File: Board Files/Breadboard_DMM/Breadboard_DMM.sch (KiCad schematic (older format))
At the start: 8 parts

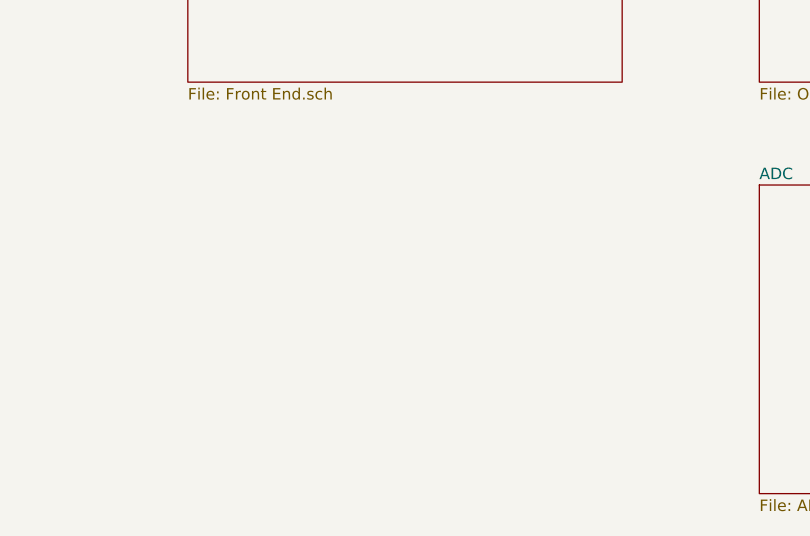
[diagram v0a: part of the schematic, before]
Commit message: Started cleaning up front end page
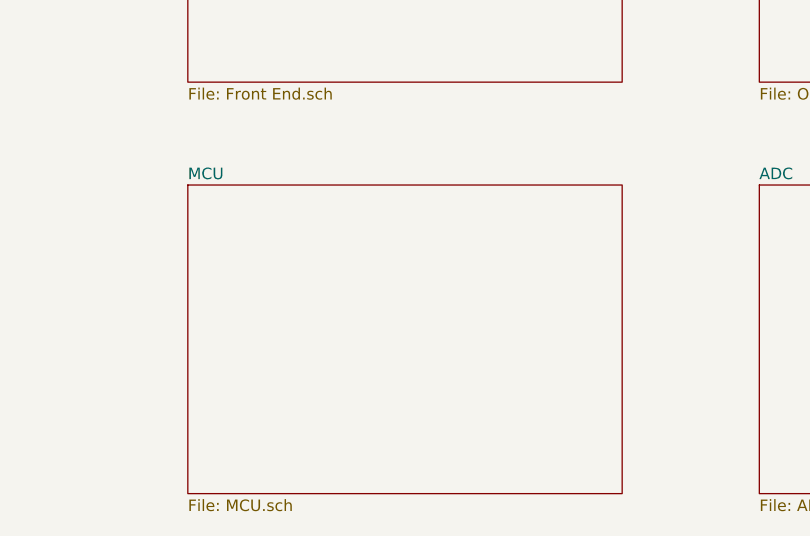
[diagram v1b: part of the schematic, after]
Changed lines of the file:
@@
 $Descr USLetter 11000 8500
 encoding utf-8
-Sheet 1 4
+Sheet 1 6
 Title "Toast-O-Meter"
 Date "2020-08-14"
@@
 F1 "ADC.sch" 50
 $EndSheet
+$Sheet
+S 1850 4700 1900 1350
+U 5F3FD151
+F0 "MCU" 50
+F1 "MCU.sch" 50
+$EndSheet
 $EndSCHEMATC

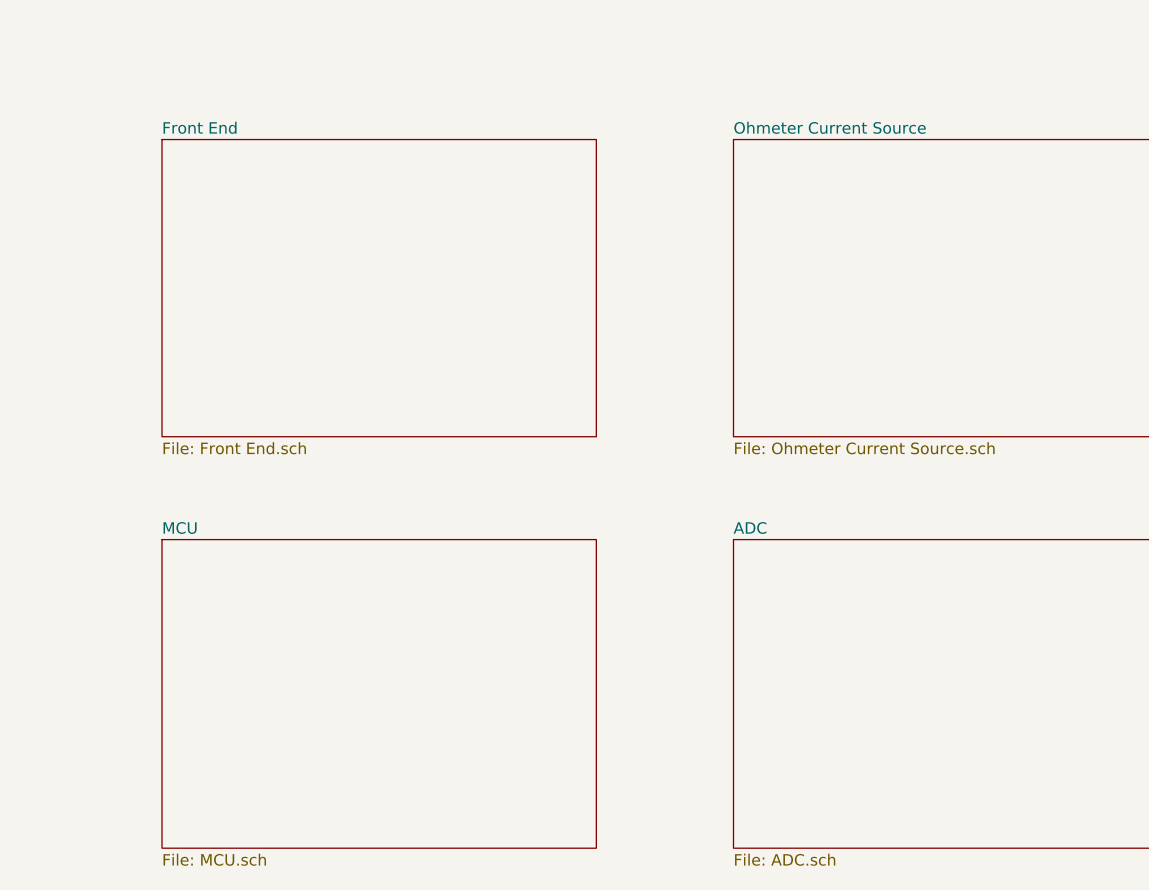
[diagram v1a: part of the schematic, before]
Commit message: Starting converting to hierachichal design
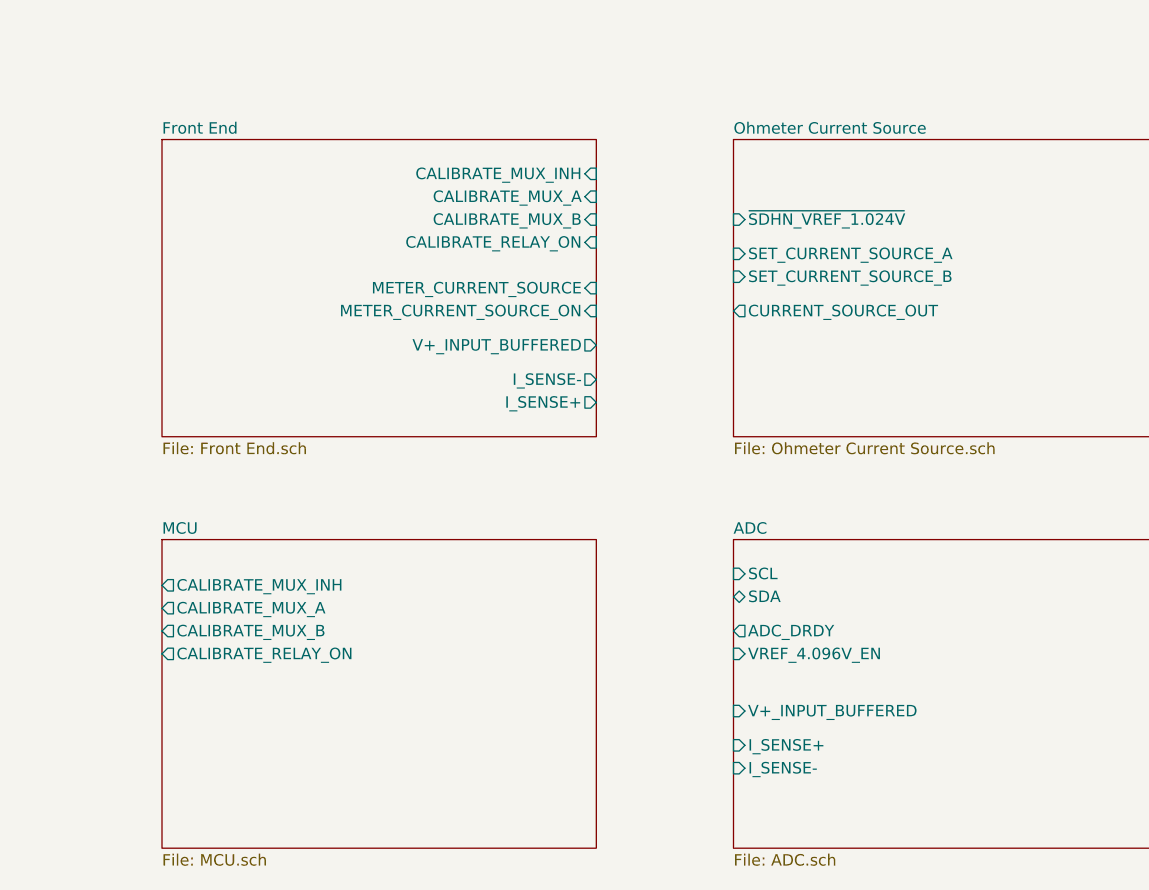
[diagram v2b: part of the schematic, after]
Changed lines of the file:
@@
 $EndComp
+$Sheet
+S 1850 4700 1900 1350
+U 5F3FD151
+F0 "MCU" 50
+F1 "MCU.sch" 50
+F2 "CALIBRATE_MUX_INH" O L 1850 4900 50
+F3 "CALIBRATE_MUX_A" O L 1850 5000 50
+F4 "CALIBRATE_MUX_B" O L 1850 5100 50
+F5 "CALIBRATE_RELAY_ON" O L 1850 5200 50
+$EndSheet
+$Sheet
+S 4350 4700 1900 1350
+U 5FDFAE85
+F0 "ADC" 50
+F1 "ADC.sch" 50
+F2 "V+_INPUT_BUFFERED" I L 4350 5450 50
+F3 "I_SENSE+" I L 4350 5600 50
+F4 "I_SENSE-" I L 4350 5700 50
+F5 "VREF_4.096V_EN" I L 4350 5200 50
+F6 "SCL" I L 4350 4850 50
+F7 "SDA" B L 4350 4950 50
+F8 "ADC_DRDY" O L 4350 5100 50
+$EndSheet
 $Sheet
 S 1850 2950 1900 1300
@@
 F0 "Front End" 50
 F1 "Front End.sch" 50
+F2 "CALIBRATE_MUX_INH" I R 3750 3100 50
+F3 "CALIBRATE_MUX_A" I R 3750 3200 50
+F4 "CALIBRATE_MUX_B" I R 3750 3300 50
+F5 "METER_CURRENT_SOURCE" I R 3750 3600 50
+F6 "V+_INPUT_BUFFERED" O R 3750 3850 50
+F7 "METER_CURRENT_SOURCE_ON" I R 3750 3700 50
+F8 "CALIBRATE_RELAY_ON" I R 3750 3400 50
+F9 "I_SENSE-" O R 3750 4000 50
+F10 "I_SENSE+" O R 3750 4100 50
 $EndSheet
 $Sheet
@@
 F0 "Ohmeter Current Source" 50
 F1 "Ohmeter Current Source.sch" 50
-$EndSheet
-$Sheet
-S 4350 4700 1900 1350
-U 5FDFAE85
-F0 "ADC" 50
-F1 "ADC.sch" 50
-$EndSheet
-$Sheet
-S 1850 4700 1900 1350
-U 5F3FD151
-F0 "MCU" 50
-F1 "MCU.sch" 50
+F2 "~SDHN_VREF_1.024V~" I L 4350 3300 50
+F3 "SET_CURRENT_SOURCE_A" I L 4350 3450 50
+F4 "SET_CURRENT_SOURCE_B" I L 4350 3550 50
+F5 "CURRENT_SOURCE_OUT" O L 4350 3700 50
 $EndSheet
 $EndSCHEMATC

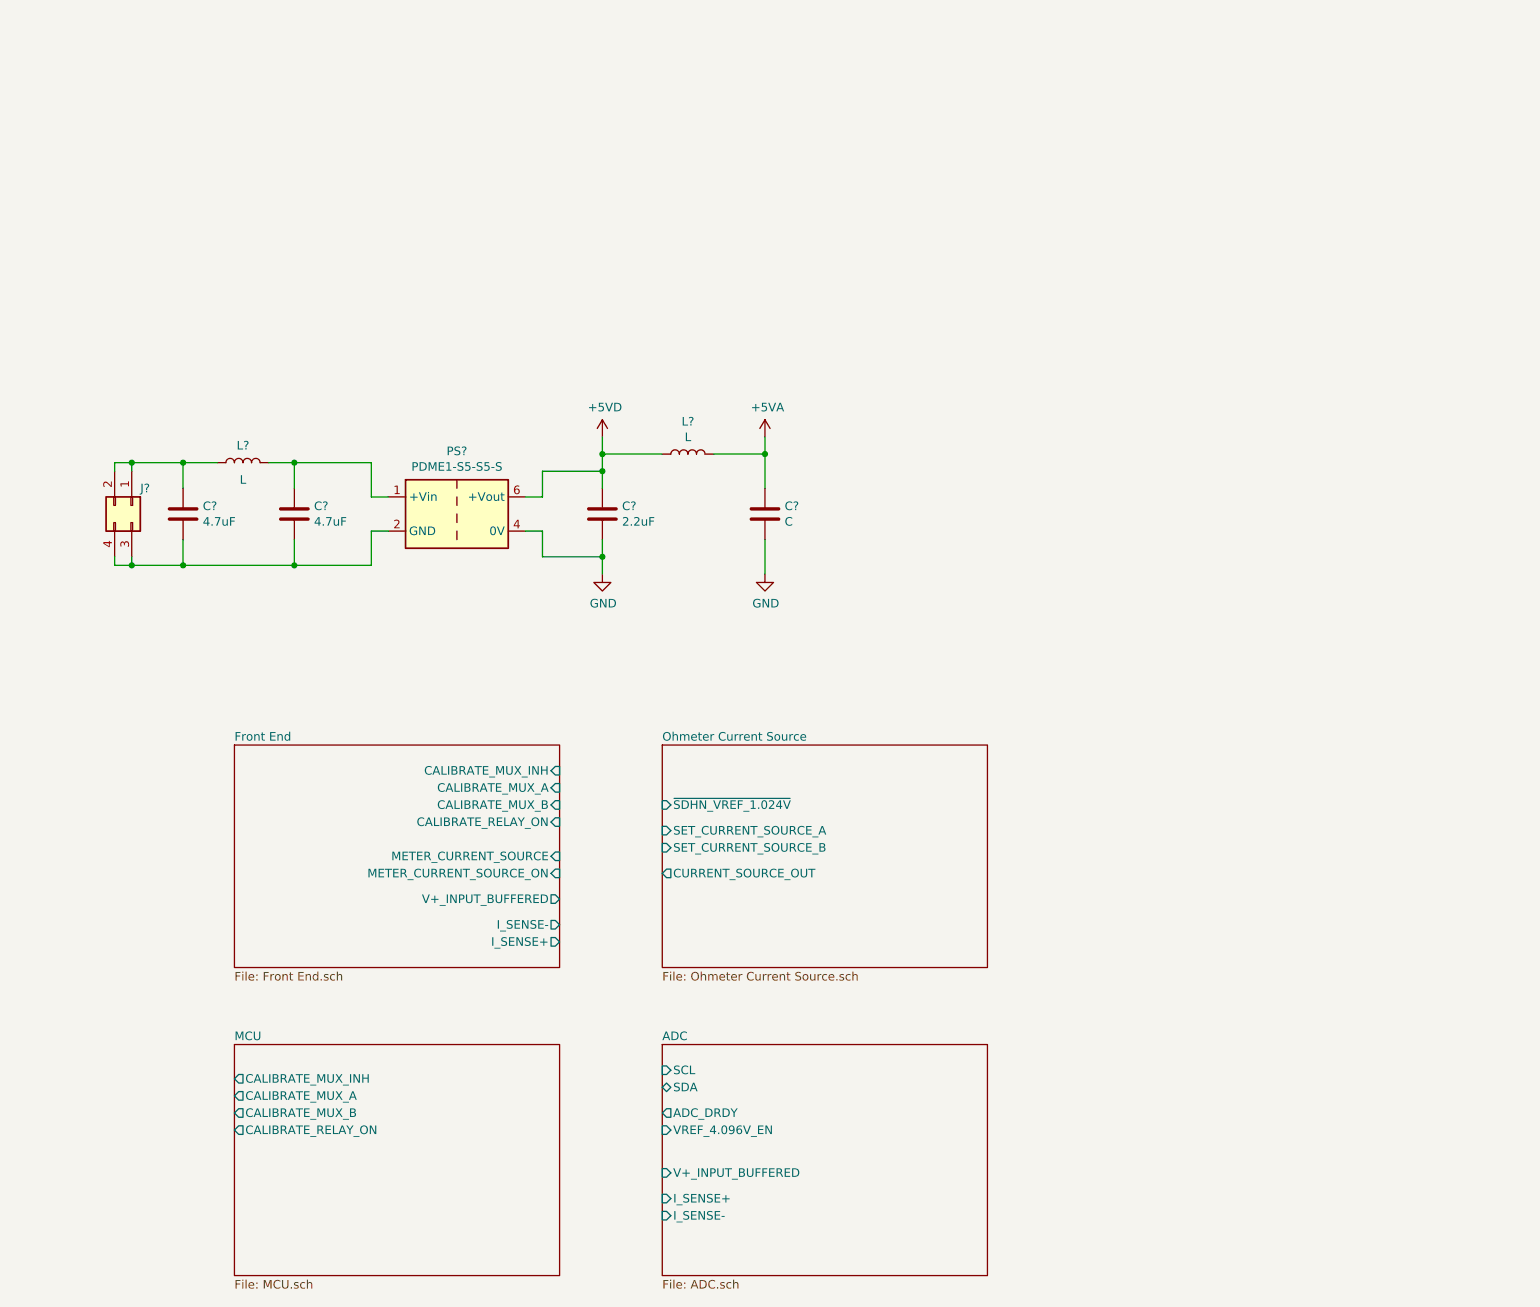
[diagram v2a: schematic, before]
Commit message: Added new sheet for main supply measurement, added upgrades document
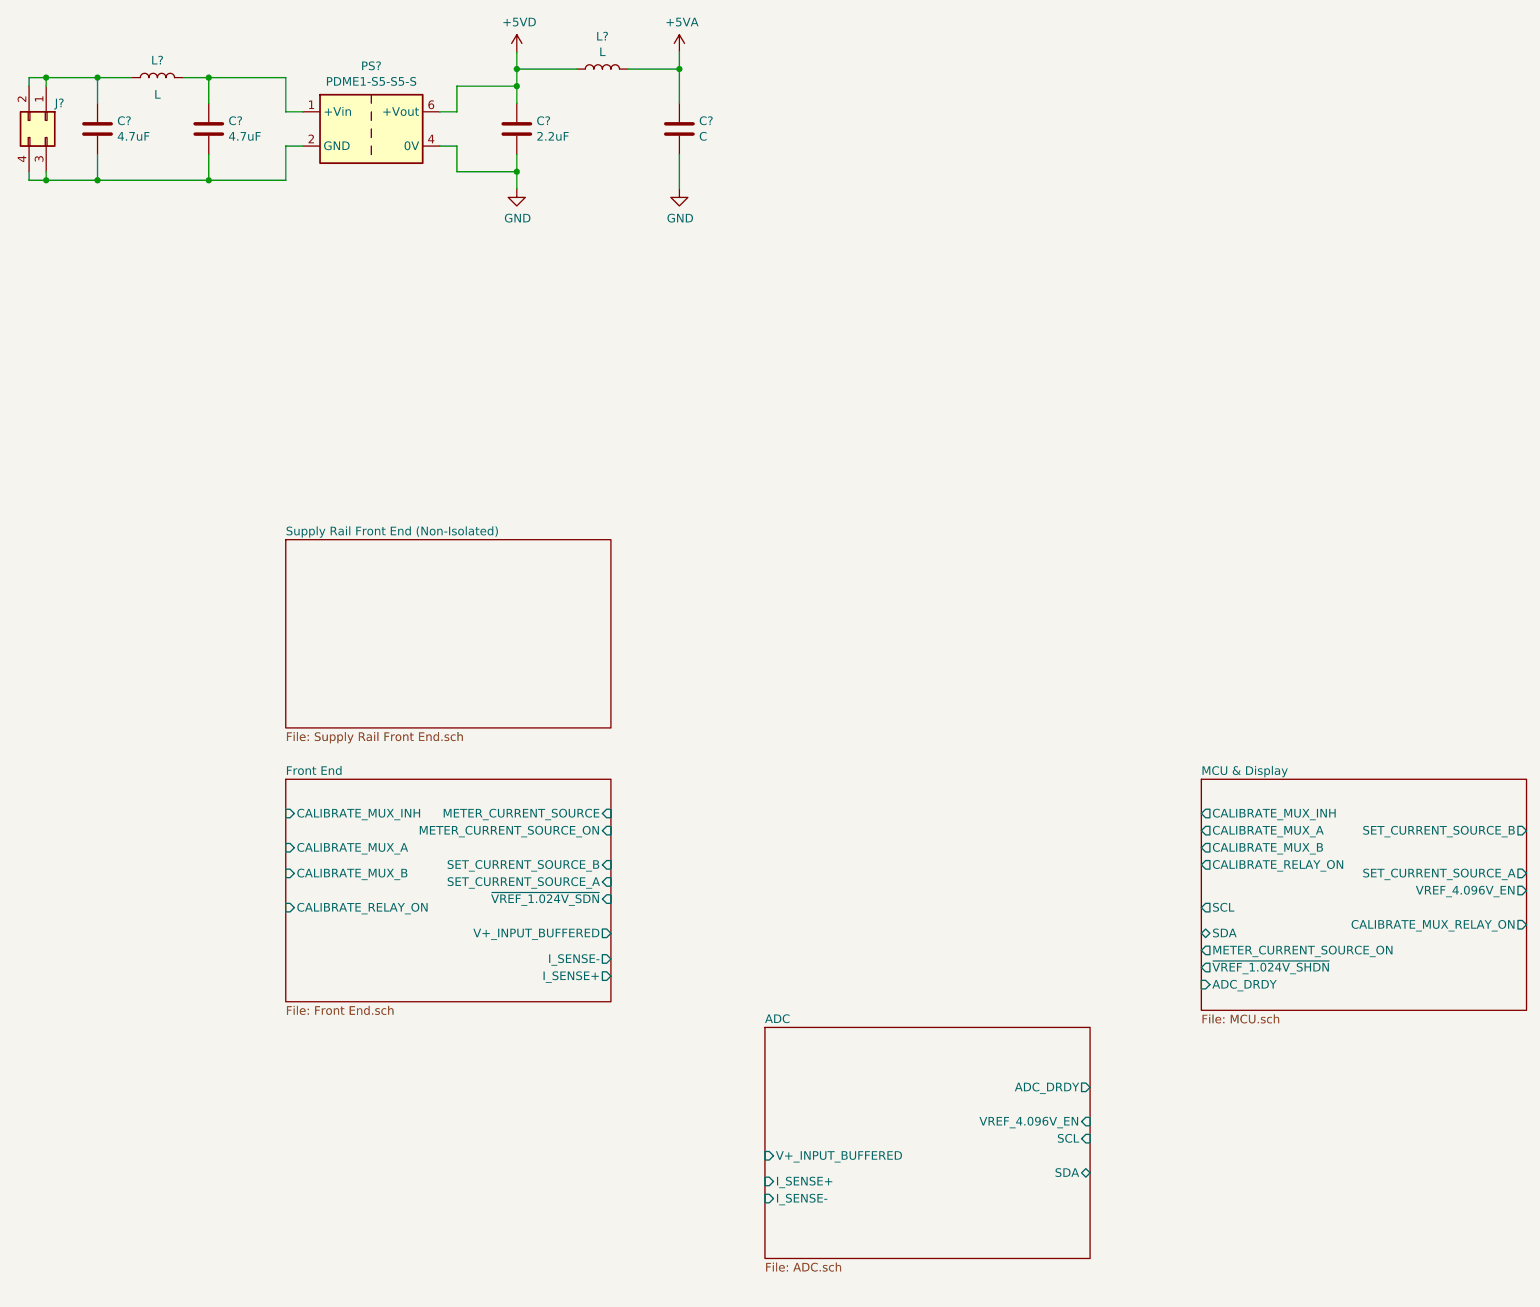
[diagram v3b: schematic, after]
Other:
- moved on the sheet: C?, J?, L?, PS?

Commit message: Finished main design, cleaning up schematic
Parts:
- removed J?: Conn_02x02_Top_Bottom, symbol Connector_Generic:Conn_02x02_Top_Bottom
- added C? (x2): 1uF, symbol Device:C
- added J?: Conn_02x03_Odd_Even, symbol Connector_Generic:Conn_02x03_Odd_Even
- added U?: MIC5365-3.3YD5, Package_TO_SOT_SMD:SOT-23-5, symbol Regulator_Linear:MIC5365-3.3YD5
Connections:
- net +5VD: now also C?.1, U?.1 (VIN), U?.3 (EN)
- net GND: now also C?.2, C?.2, U?.2 (GND)
- net Power Input Protection/V_OUT+: now reaches C?.1, L?.1
- net Power Input Protection/V_OUT-: now reaches C?.2, C?.2, PS?.2 (GND)
- new net +3V3: C?.1, U?.5 (VOUT)
- new net Power Input Protection/V_IN+: J?.2 (Pin_2), J?.4 (Pin_4), J?.6 (Pin_6)
- new net Power Input Protection/V_IN-: J?.1 (Pin_1), J?.3 (Pin_3), J?.5 (Pin_5)
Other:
- moved on the sheet: C?, L?, PS?
